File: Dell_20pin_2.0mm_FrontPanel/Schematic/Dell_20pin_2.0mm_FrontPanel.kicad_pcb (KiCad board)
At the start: 2 copper layers, 36.8 x 14.5 mm, 6 parts, among them J1 DELL_2MM_MB_CONNECTOR, J2 HDD_LED_HEADER, J3 Conn_01x04, J4 HDAUDIO_HEADER, J5 Conn_01x05

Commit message: start new PCB design
For some reason, when I load the original one in
pcbnew, it does not show any tracks, but also does
any rats nest connections.
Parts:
- J1, R1: moved to F.Cu
- moved J2 29.1 mm to (146.9, 109.2), turned to 0 degrees
- moved R1 20.3 mm to (151.4, 108.4), turned to 0 degrees
- moved J1 20.2 mm to (142.5, 94.1), turned to 0 degrees
- moved J5 8.09 mm to (154.1, 94.4), turned to 0 degrees
- moved J4 7.95 mm to (146.9, 94.4), turned to 0 degrees
- moved J3 7.36 mm to (158.7, 94.4), turned to 0 degrees
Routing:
- net FRONT_IO_DET: track 48.2 -> 0.00 mm
- net USB_D+_1: track 45.4 -> 0.00 mm
- net USB_VCC1: track 44.1 -> 0.00 mm
- net USB_D-_1: track 42.8 -> 0.00 mm
- net HEADPHONE_L: track 32.5 -> 0.00 mm
- net MIC_L: track 32.0 -> 0.00 mm
- net MIC_DET: track 29.1 -> 0.00 mm
- net MIC_R: track 20.8 -> 0.00 mm
- net USB_D+_2: track 18.8 -> 0.00 mm, vias 1 -> 0
- net HDD_LED-: track 18.6 -> 0.00 mm
- net USB_D-_2: track 15.5 -> 0.00 mm
- net HEADPHONE_R: track 13.8 -> 0.00 mm
- net HDD_LED+: track 13.1 -> 0.00 mm, vias 1 -> 0
- net USB_VCC2: track 10.1 -> 0.00 mm
- net HEADPHONE_DET: track 8.77 -> 0.00 mm
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- removed copper zone on B.Cu, net FRONT_IO_DET
- removed copper zone on F.Cu, net FRONT_IO_DET
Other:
- board outline removed
- net class Default: trace_width 0.35 -> 0.25
- board text removed: "- +"
- board text removed: "HDD LED"
- board text removed: "HD_AUDIO"
- board text removed: "Motherboard Side"
- board text removed: "OPTIPLEX 7010 7020 9010 9020 FP ADAPTER"
- board text removed: "USB 2.0"
- board text removed: "github.com/ harbinrepairs"

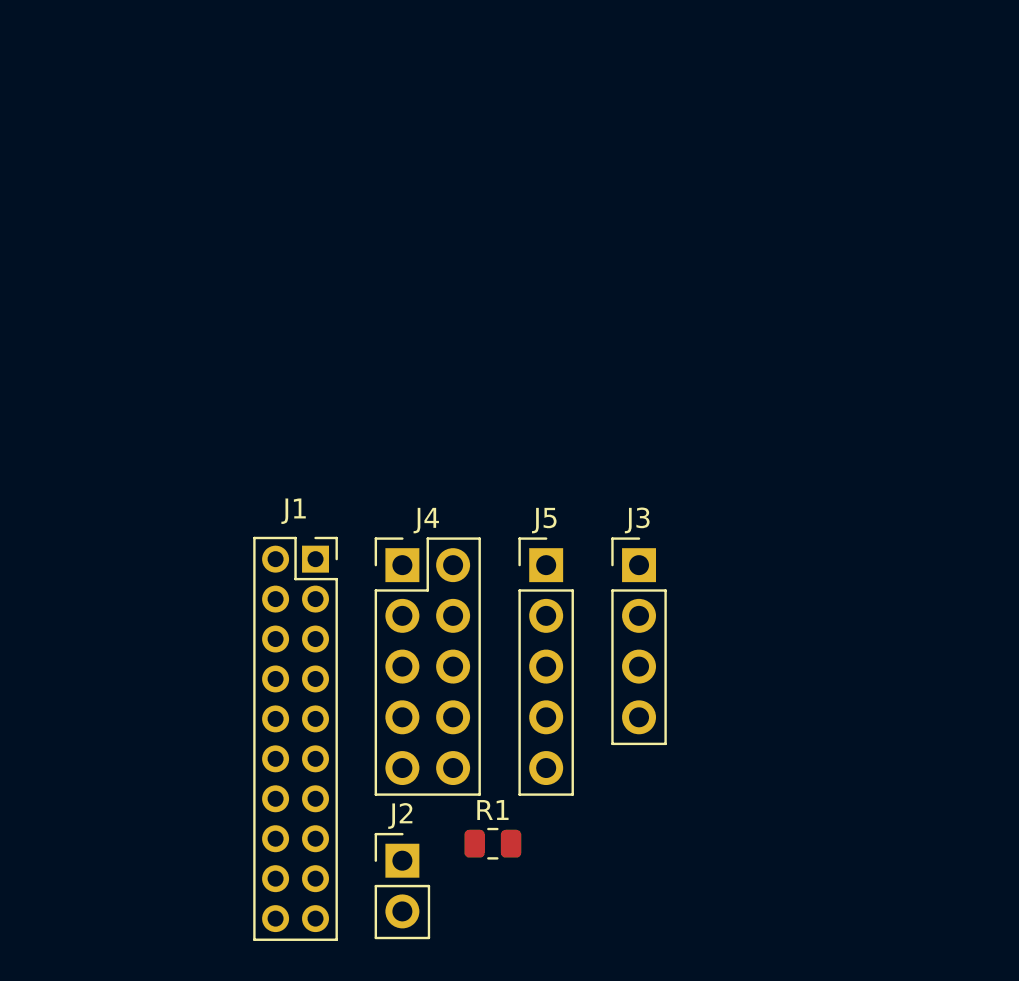
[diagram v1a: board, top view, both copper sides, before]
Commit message: placed components
Note that I still need to make a cutout to avoid
obstructing the connector for the temperature sensor.
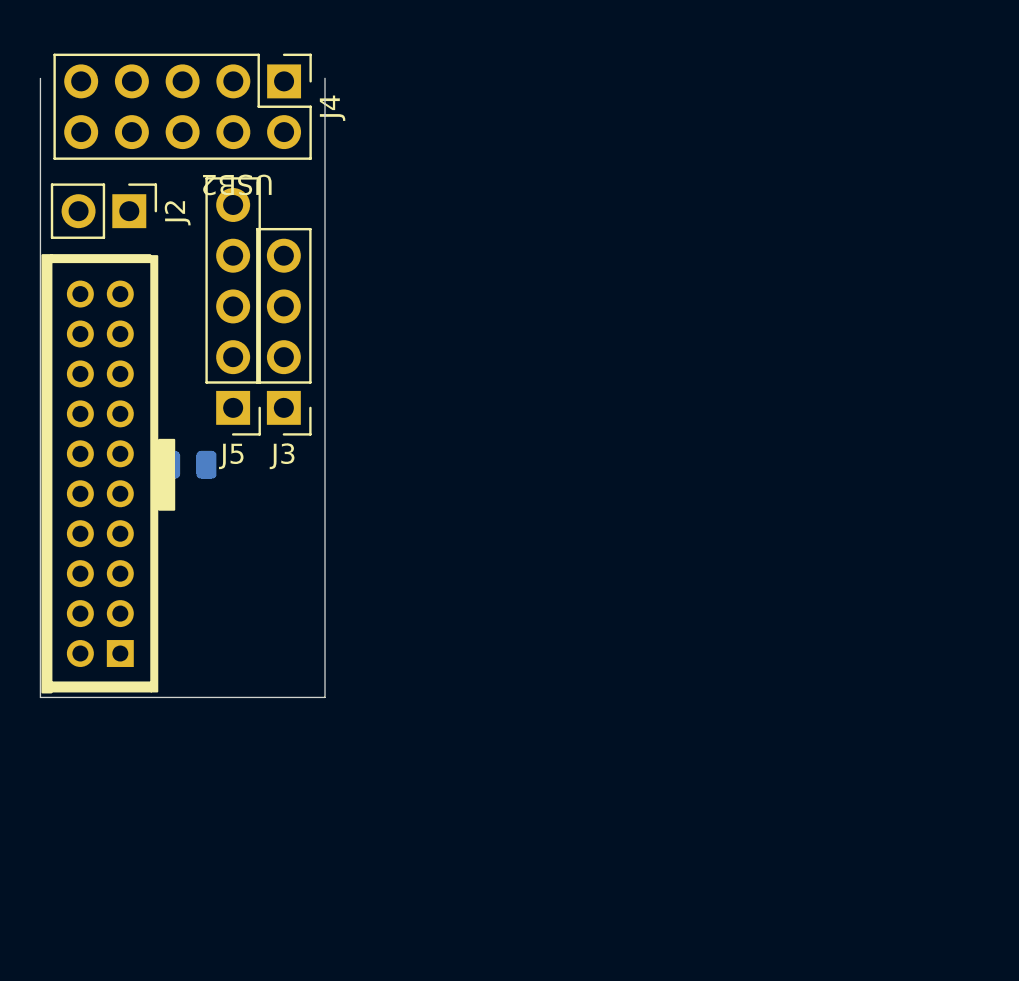
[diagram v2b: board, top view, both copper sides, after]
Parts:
- J1, R1: moved to B.Cu
- moved J2 35.3 mm to (133.2, 76.7), turned to 270 degrees
- moved J4 24.9 mm to (140.9, 70.2), turned to 270 degrees
- moved R1 24.3 mm to (136.2, 89.4)
- moved J3 19.5 mm to (140.9, 86.5), turned to 180 degrees
- moved J5 17.5 mm to (138.4, 86.5), turned to 180 degrees
- moved J1 10.9 mm to (132.8, 98.8)
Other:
- board outline added: 14.2 x 31 mm
- board text added: "USB2"

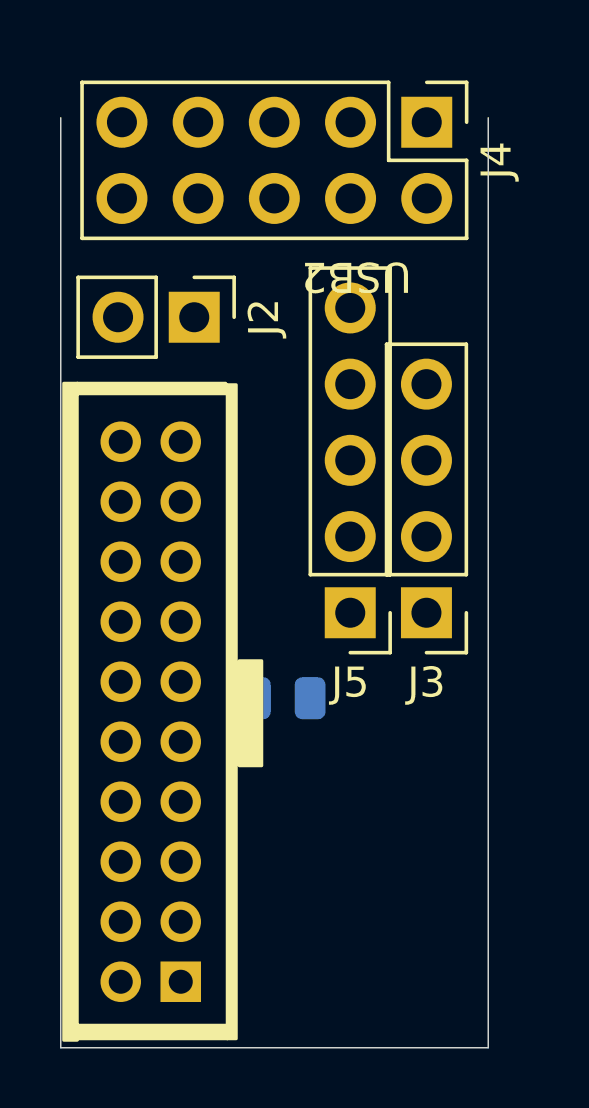
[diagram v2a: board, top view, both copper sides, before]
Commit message: added cutout for temp sensor connector
also, set up design rules for OSHPark, and start
routing
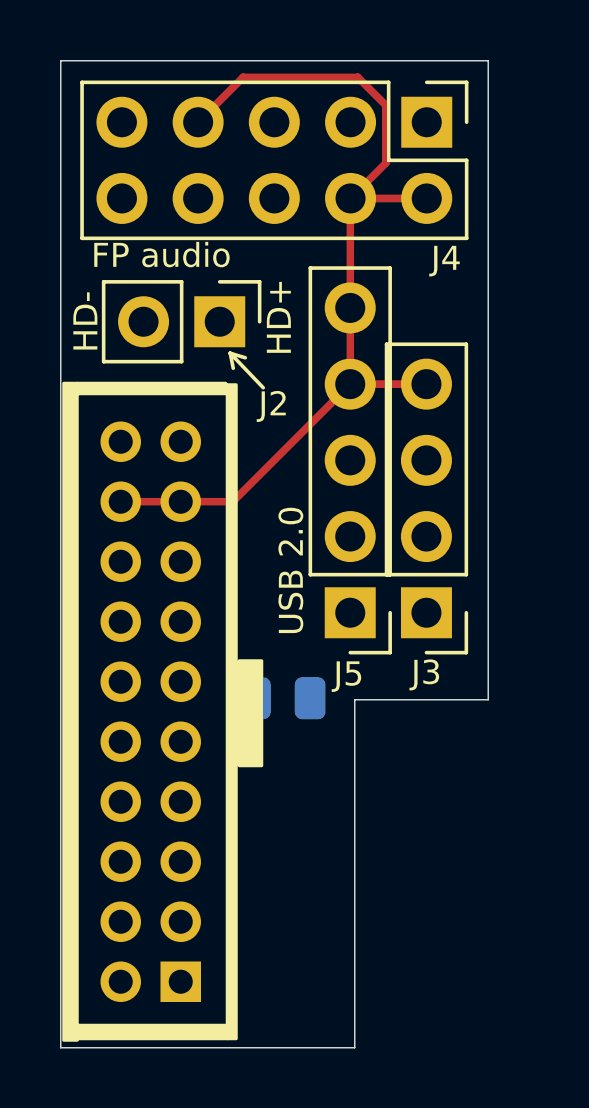
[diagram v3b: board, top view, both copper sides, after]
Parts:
- moved J2 0.86 mm to (134.1, 76.8)
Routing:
- net FRONT_IO_DET: track 0.00 -> 31.4 mm
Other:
- board size 14.2 x 31 mm -> 14.2 x 32.9 mm
- board text added: "FP audio"
- board text added: "HD+"
- board text added: "HD-"
- board text added: "USB 2.0"
- board text removed: "USB2"

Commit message: all traces routed?
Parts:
- moved R1 2.30 mm to (135.3, 91.5), turned to 90 degrees
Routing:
- net MIC_R: track 0.00 -> 41.4 mm
- net MIC_L: track 0.00 -> 38.2 mm
- net HEADPHONE_L: track 0.00 -> 34.4 mm
- net HEADPHONE_R: track 0.00 -> 32.7 mm, vias 0 -> 1
- net MIC_DET: track 0.00 -> 28.5 mm
- net HEADPHONE_DET: track 0.00 -> 25.3 mm
- net HDD_LED-: track 0.00 -> 14.5 mm
- net Net-(J2-Pad1): track 0.00 -> 14.3 mm
- net FRONT_IO_DET: track 31.4 -> 44.5 mm
- net USB_D+_1: track 0.00 -> 9.59 mm
- net USB_D-_1: track 0.00 -> 9.37 mm
- net USB_VCC1: track 0.00 -> 9.14 mm
- net USB_D+_2: track 0.00 -> 9.05 mm
- net USB_D-_2: track 0.00 -> 8.83 mm
- net USB_VCC2: track 0.00 -> 8.60 mm
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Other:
- board text added: "Bottom"
- board text added: "Top"

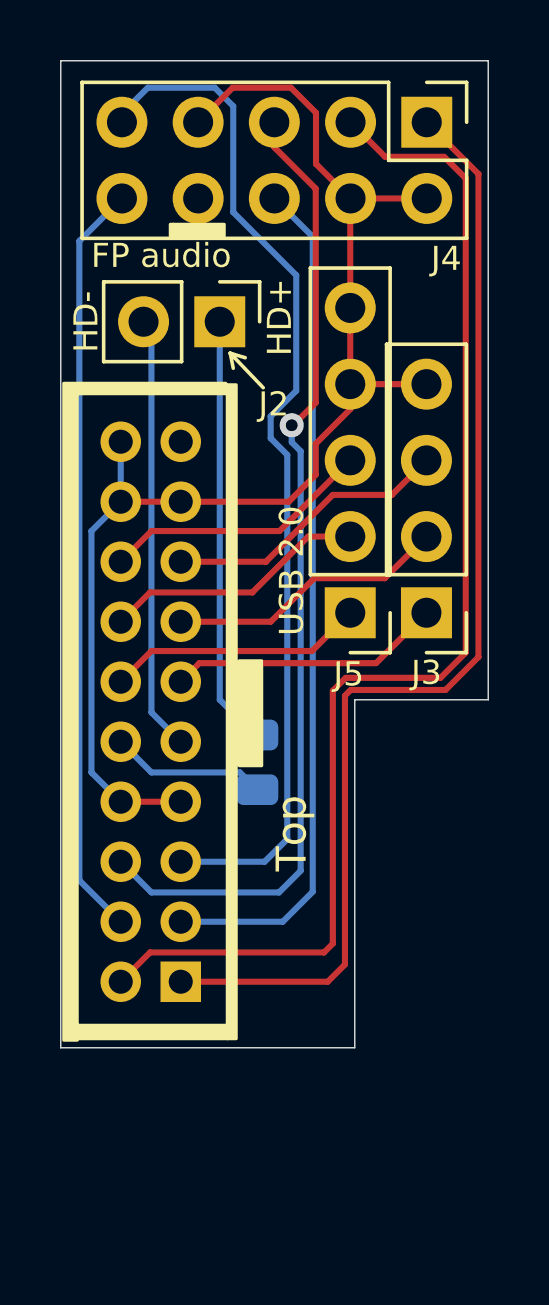
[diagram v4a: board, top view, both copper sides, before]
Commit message: move front-panel USB2 connector
In the previous version, the part of the PCB where the
USB2 connector was located bumped up against a capacitor
on the motherboard. In the revised version, the
USB2 connector is moved to the "bottom" of the adapter
PCB, so the cutout can extended to accommodate the
capacitor.

I think the adapter will hang off the edge of the
motherboard slightly towards the "bottom" of
the adapter PCB, but this edge of the motherboard
aligns with the front of the case, and I have never
seen a case that fits the motherboard flush with
the front of the case.
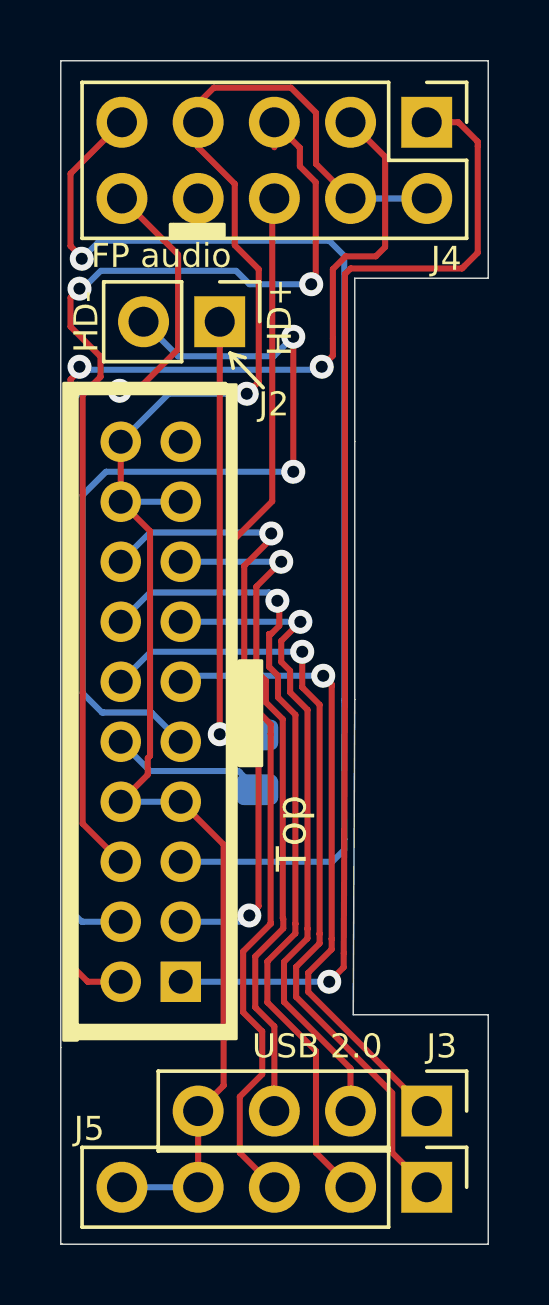
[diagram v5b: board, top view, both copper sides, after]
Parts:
- moved J5 19.3 mm to (140.9, 105.7), turned to 270 degrees
- moved J3 16.6 mm to (140.9, 103.2), turned to 270 degrees
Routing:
- net USB_D+_2: track 9.05 -> 29.4 mm, vias 0 -> 1
- net USB_D-_2: track 8.83 -> 27.4 mm, vias 0 -> 1
- net USB_VCC2: track 8.60 -> 26.7 mm, vias 0 -> 1
- net FRONT_IO_DET: track 44.5 -> 59.1 mm, vias 0 -> 1
- net HDD_LED-: track 14.5 -> 28.3 mm, vias 0 -> 2
- net USB_D+_1: track 9.59 -> 23.0 mm, vias 0 -> 1
- net USB_D-_1: track 9.37 -> 22.5 mm, vias 0 -> 1
- net USB_VCC1: track 9.14 -> 21.8 mm, vias 0 -> 1
- net HEADPHONE_L: track 34.4 -> 40.3 mm, vias 0 -> 1
- net HEADPHONE_DET: track 25.3 -> 28.9 mm, vias 0 -> 1
- net HEADPHONE_R: track 32.7 -> 35.5 mm, vias 1 -> 2
- net MIC_R: track 41.4 -> 40.2 mm, vias 0 -> 2
- net MIC_DET: track 28.5 -> 27.3 mm, vias 0 -> 1
- net MIC_L: track 38.2 -> 39.1 mm, vias 0 -> 1
- net Net-(J2-Pad1): track 14.3 -> 15.1 mm, vias 0 -> 1
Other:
- board size 14.2 x 32.9 mm -> 14.2 x 39.4 mm
